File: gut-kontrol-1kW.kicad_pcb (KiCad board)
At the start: 2 copper layers, 119 x 85 mm, 49 parts, among them J1 PHASE_A, J2 PHASE_B, J3 PHASE_C, J4 VMOT, J5 GND, J7 Conn_01x12, Q1 IRFb4110N, Q2 IRFb4110N, Q3 IRFb4110N, Q4 IRFb4110N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

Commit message: Adding connector and CAD viz
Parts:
- added C11: 0.1 uF, Capacitor_SMD:C_0805_2012Metric_Pad1.18x1.45mm_HandSolder, F.Cu at (51.8, 59.1)
- added C12: 0.1 uF, Capacitor_SMD:C_0805_2012Metric_Pad1.18x1.45mm_HandSolder, F.Cu at (81.8, 59.1)
- added C13: 0.1 uF, Capacitor_SMD:C_0805_2012Metric_Pad1.18x1.45mm_HandSolder, F.Cu at (111.8, 59.1)
- added C14: 0.1 uF, Capacitor_SMD:C_0805_2012Metric_Pad1.18x1.45mm_HandSolder, F.Cu at (47.0, 59.7)
- added C15: 0.1 uF, Capacitor_SMD:C_0805_2012Metric_Pad1.18x1.45mm_HandSolder, F.Cu at (77.0, 59.7)
- added C16: 0.1 uF, Capacitor_SMD:C_0805_2012Metric_Pad1.18x1.45mm_HandSolder, F.Cu at (107.0, 59.7)
- added G***: LOGO, symbols:gut_25mm, F.Cu at (116.5, 119.2)
- added J10: PHASE_C_ISENSE, Connector_PinSocket_2.54mm:PinSocket_1x03_P2.54mm_Vertical, F.Cu at (108.3, 55.9)
- added J8: PHASE_A_ISENSE, Connector_PinSocket_2.54mm:PinSocket_1x03_P2.54mm_Vertical, F.Cu at (48.3, 55.9)
- added J9: PHASE_B_ISENSE, Connector_PinSocket_2.54mm:PinSocket_1x03_P2.54mm_Vertical, F.Cu at (78.3, 55.9)
- added R16: 100, Resistor_SMD:R_0805_2012Metric_Pad1.20x1.40mm_HandSolder, F.Cu at (49.5, 62.2)
- added R17: 100, Resistor_SMD:R_0805_2012Metric_Pad1.20x1.40mm_HandSolder, F.Cu at (79.5, 62.2)
- added R18: 100, Resistor_SMD:R_0805_2012Metric_Pad1.20x1.40mm_HandSolder, F.Cu at (109.5, 62.2)
- R15: renamed from R10; value 27 -> 10K
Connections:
- R15 pad 1: Net-(R10-Pad1) -> GND
- R15 pad 2: Net-(Q5-Pad1) -> Net-(Q6-Pad1)
- U2 pad 3: A_CURRENT_SENS -> Net-(R16-Pad1)
- U5 pad 3: B_CURRENT_SENS -> Net-(R17-Pad1)
- U6 pad 3: C_CURRENT_SENS -> Net-(R18-Pad1)
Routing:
- net Net-(R18-Pad1): track 0.00 -> 14.1 mm
- net Net-(R17-Pad1): track 0.00 -> 14.1 mm
- net Net-(R16-Pad1): track 0.00 -> 14.1 mm
- net GND: track 33.8 -> 43.6 mm, vias 13 -> 20
- net Net-(C13-Pad2): track 0.00 -> 6.43 mm
- net Net-(C11-Pad2): track 0.00 -> 6.43 mm
- net Net-(C12-Pad2): track 0.00 -> 6.43 mm
- net Net-(R11-Pad1): track 0.00 -> 4.54 mm
- net Net-(R10-Pad1): track 1.62 -> 4.79 mm, vias 1 -> 0
- net /PHASE_B: track 8.13 -> 7.33 mm
- net +48V: vias 0 -> 41
- added copper zone on B.Cu, net /PHASE_A_OUT
- added copper zone on B.Cu, net /PHASE_B_OUT
- added copper zone on B.Cu, net /PHASE_C_OUT
- added copper zone on F.Cu, net GND
- added copper zone on F.Cu, net HIN_A
- added copper zone on F.Cu, net HIN_B
- added copper zone on F.Cu, net HIN_C
- added copper zone on F.Cu, net LIN_A
- added copper zone on F.Cu, net LIN_B
- added copper zone on F.Cu, net LIN_C
- added copper zone on F.Cu, net Net-(C11-Pad2)
- added copper zone on F.Cu, net Net-(C12-Pad2)
- added copper zone on F.Cu, net Net-(C13-Pad2)
- added copper zone on F.Cu, net Net-(Q1-Pad1)
- added copper zone on F.Cu, net Net-(Q2-Pad1)
- added copper zone on F.Cu, net Net-(Q3-Pad1)
- added copper zone on F.Cu, net Net-(Q4-Pad1)
- added copper zone on F.Cu, net Net-(Q5-Pad1)
- added copper zone on F.Cu, net Net-(Q6-Pad1)
- added copper zone on F.Cu, net Net-(R16-Pad1)
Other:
- outline, holes or cut-outs redrawn
- board text added: "+ 3V3"
- board text added: "+12V"
- board text added: "A PWM"
- board text added: "B PWM"
- board text added: "C PWM"
- board text added: "GATE DRIVER"
- board text added: "GND"
- board text added: "GUT-KONTROL-1KW-v0.1 POWERSTAGE BOARD"

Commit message: some minor fix
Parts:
- C4: renamed from C6; value 2.2 uF -> 10 uF
- C5: renamed from C3; value 10 uF -> 2.2 uF
- R10: renamed from R12; value 10K -> 27
- R11: renamed from R13; value 10K -> 27
- renumbered C4 to C3, C5 to C6, R15 to R13, R8 to R9
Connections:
- C4 pad 1: /PHASE_C -> GND
- C4 pad 2: Net-(C6-Pad2) -> +3V3
- C5 pad 1: GND -> /PHASE_B
- C5 pad 2: +3V3 -> Net-(C5-Pad2)
- C6 pad 1: /PHASE_B -> /PHASE_C
- C6 pad 2: Net-(C5-Pad2) -> Net-(C6-Pad2)
- R10 pad 1: /PHASE_B -> Net-(R10-Pad1)
- R10 pad 2: Net-(Q3-Pad1) -> Net-(Q5-Pad1)
- R11 pad 1: GND -> Net-(R11-Pad1)
- R11 pad 2: Net-(Q4-Pad1) -> Net-(Q6-Pad1)
- R13 pad 2: Net-(Q6-Pad1) -> Net-(Q4-Pad1)
- R9 pad 1: Net-(R8-Pad1) -> Net-(R9-Pad1)
- R9 pad 2: Net-(Q3-Pad1) -> Net-(Q4-Pad1)
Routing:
- net +3V3: track 9.70 -> 23.9 mm, vias 0 -> 2
- net (no net): track 0.00 -> 8.50 mm, vias 0 -> 4
- net /PHASE_B: track 7.33 -> 9.55 mm
- net /PHASE_A: track 7.67 -> 9.89 mm
- net GND: track 43.6 -> 45.2 mm, vias 20 -> 21
- net /PHASE_C: track 8.94 -> 9.55 mm, vias 1 -> 0
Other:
- board text removed: "+ 3V3"
- board text removed: "+12V"
- board text removed: "A PWM"
- board text removed: "B PWM"
- board text removed: "C PWM"
- board text removed: "GND"

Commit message: major fix in conn footprint, bootsrap error, etc
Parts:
- removed the REF** at (105.0, 110.0)
- added U7: XT30PW-F, XT30PW-F:XT30PW-F, F.Cu at (156.6, 233.8)
- J7: footprint Connector_PinHeader_1.00mm:PinHeader_1x12_P1.00mm_Vertical -> Connector_PinHeader_2.54mm:PinHeader_1x12_P2.54mm_Vertical
- moved C1 165.1 mm to (173.8, 215.5)
- moved C10 165.0 mm to (257.1, 240.3)
- moved C11 165.0 mm to (165.9, 178.3)
- moved C12 165.0 mm to (195.9, 178.3)
- moved C13 165.0 mm to (225.9, 178.3)
- moved C2 165.0 mm to (173.1, 231.7)
- moved C3 165.0 mm to (203.1, 231.7)
- moved C5 165.0 mm to (203.8, 215.4)
- moved C6 165.0 mm to (233.8, 215.4)
- moved C7 165.0 mm to (257.1, 180.3)
- moved C8 165.0 mm to (257.1, 200.3)
- moved C9 165.0 mm to (257.1, 220.3)
- moved G*** 165.0 mm to (230.6, 238.5)
- moved J10 165.0 mm to (222.4, 175.2)
- moved J4 165.0 mm to (158.1, 205.3)
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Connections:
- J7 pad 1: +12V -> +3V3
- J7 pad 2: +12V -> +3V3
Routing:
- net +3V3: track 23.9 -> 11.9 mm, vias 2 -> 0
- net (no net): track 8.50 -> 0.00 mm, vias 4 -> 0
- net GND: track 45.2 -> 53.5 mm, vias 21 -> 24
- net HIN_A: track 37.3 -> 29.3 mm, vias 0 -> 2
- net LIN_A: track 36.2 -> 29.5 mm, vias 0 -> 2
- net +12V: track 56.5 -> 50.9 mm
- net HIN_C: track 38.2 -> 41.2 mm, vias 0 -> 2
- net HIN_B: track 16.6 -> 18.8 mm
- net Net-(D2-K): track 10.6 -> 12.7 mm
- net Net-(D3-K): track 10.6 -> 12.3 mm
- net LIN_B: track 17.2 -> 18.8 mm
- net Net-(D1-K): track 10.6 -> 11.8 mm
- net Net-(D2-A): track 3.44 -> 2.28 mm
- net Net-(D1-A): track 3.44 -> 2.28 mm
- net LIN_C: track 39.7 -> 40.5 mm, vias 0 -> 2
- removed copper zone on F.Cu, net HIN_A
- removed copper zone on F.Cu, net HIN_B
- removed copper zone on F.Cu, net HIN_C
- removed copper zone on F.Cu, net LIN_A
- removed copper zone on F.Cu, net LIN_B
- removed copper zone on F.Cu, net LIN_C
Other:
- board text added: "GUT-KONTROL-1KW-v0.2 POWERSTAGE BOARD"
- board text removed: "GUT-KONTROL-1KW-v0.1 POWERSTAGE BOARD"

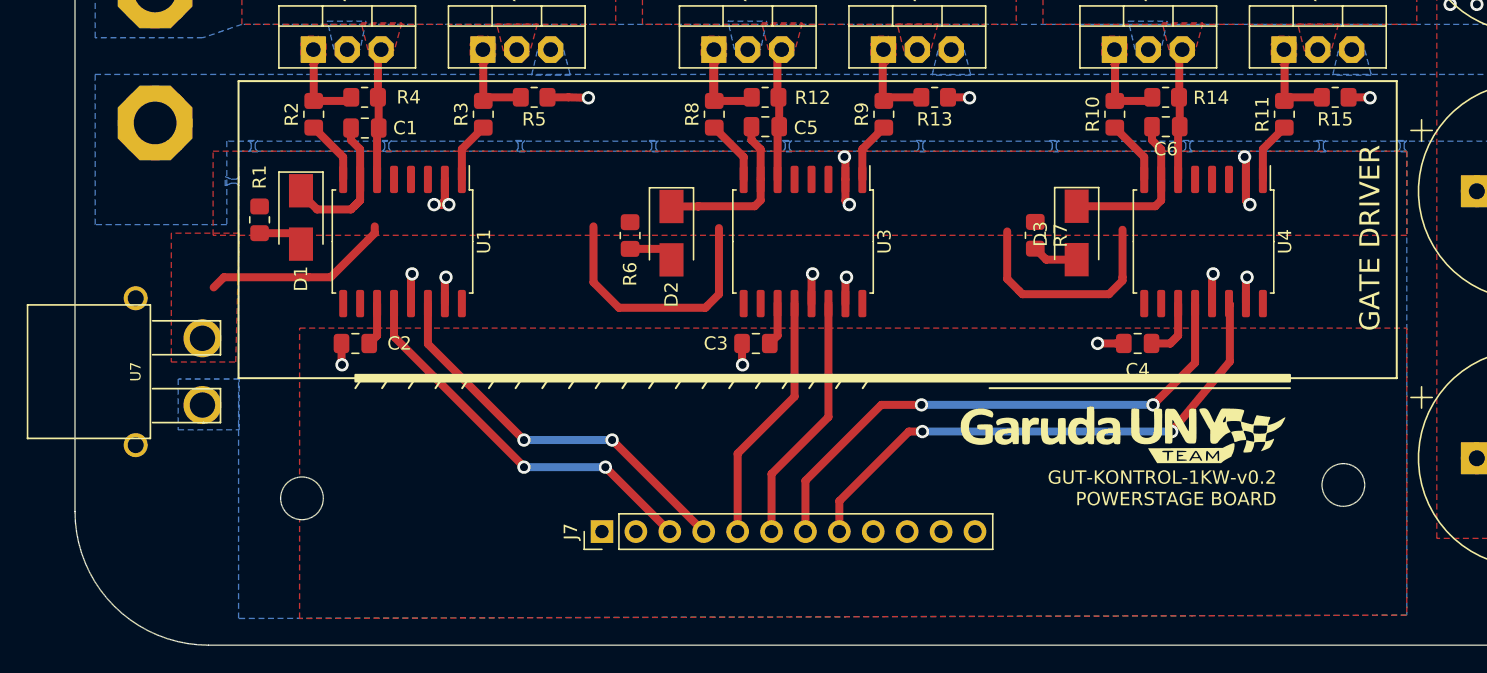
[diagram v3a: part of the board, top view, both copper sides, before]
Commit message: ganti heatsink
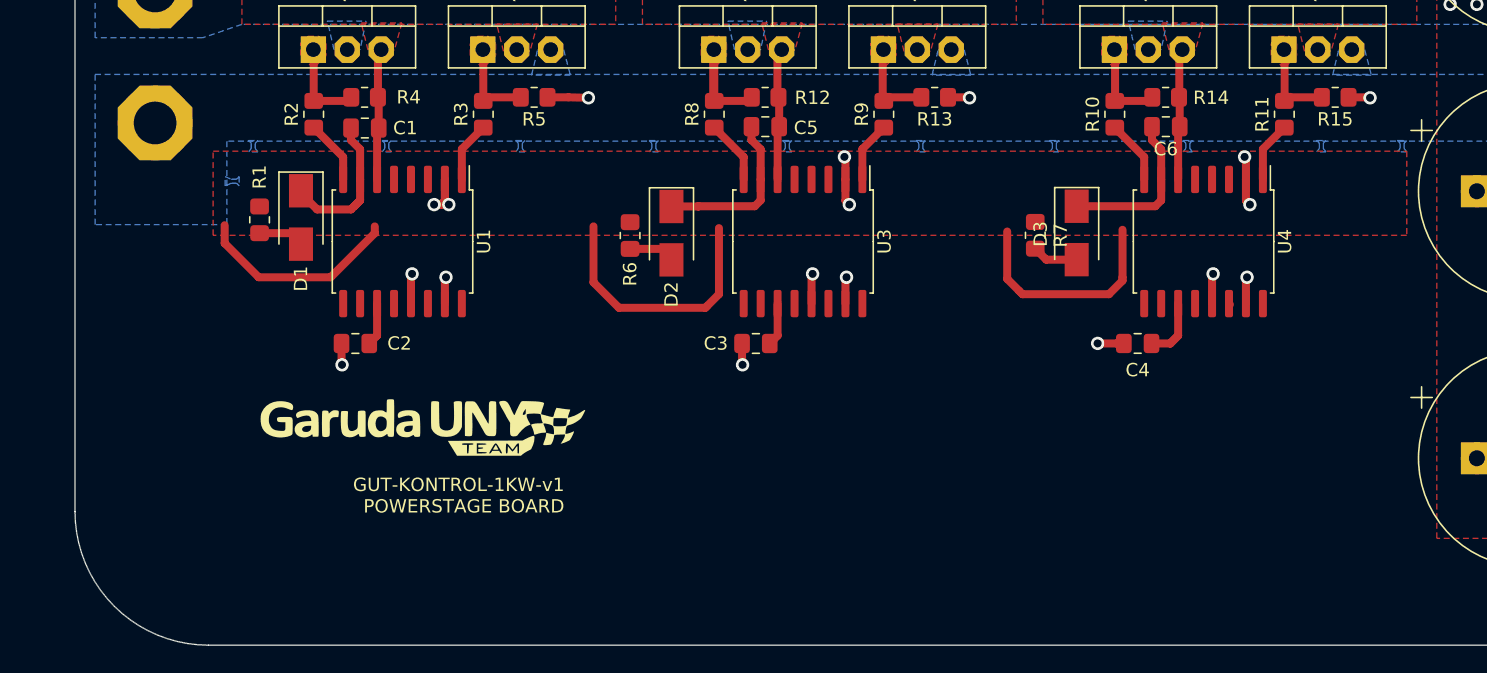
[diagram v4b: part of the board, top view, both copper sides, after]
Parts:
- removed J7: Conn_01x12, Connector_PinHeader_2.54mm:PinHeader_1x12_P2.54mm_Vertical
- removed REF** (x2): MountingHole_3.2mm_M3, MountingHole:MountingHole_3.2mm_M3
- removed U7: XT30PW-F, XT30PW-F:XT30PW-F
- moved G*** 52.4 mm to (178.2, 237.9)
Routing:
- net HIN_C: track 41.2 -> 0.00 mm, vias 2 -> 0
- net LIN_C: track 40.5 -> 0.09 mm, vias 2 -> 0
- net LIN_A: track 29.5 -> 0.00 mm, vias 2 -> 0
- net HIN_A: track 29.3 -> 0.00 mm, vias 2 -> 0
- net LIN_B: track 18.8 -> 0.00 mm
- net HIN_B: track 18.8 -> 0.00 mm
- net +12V: track 50.9 -> 52.2 mm
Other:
- board text added: "GUT-KONTROL-1KW-v1 POWERSTAGE BOARD"
- board text removed: "GATE DRIVER"
- board text removed: "GUT-KONTROL-1KW-v0.2 POWERSTAGE BOARD"

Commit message: Layout PCB
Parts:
- added ?: MountingHole_3.2mm_M3, MountingHole:MountingHole_3.2mm_M3, F.Cu at (248.3, 183.7)
- added ?: MountingHole_3.2mm_M3, MountingHole:MountingHole_3.2mm_M3, F.Cu at (156.3, 183.7)
- added ?: MountingHole_3.2mm_M3, MountingHole:MountingHole_3.2mm_M3, F.Cu at (248.3, 247.7)
- added ?: MountingHole_3.2mm_M3, MountingHole:MountingHole_3.2mm_M3, F.Cu at (160.8, 247.7)
- added CFF1: 33nF, Resistor_SMD:R_0805_2012Metric, F.Cu at (223.3, 249.0)
- added CIN1: 33uF/100W, Capacitor_THT:CP_Radial_D8.0mm_P3.50mm, F.Cu at (247.4, 240.9)
- added COUT1: 100uF/35V, Capacitor_THT:CP_Radial_D8.0mm_P3.50mm, F.Cu at (210.8, 241.0)
- added D4: S310, Diode_SMD:D_SMA, F.Cu at (236.7, 236.5)
- added J7: Conn_01x12, Connector_PinHeader_2.54mm:PinHeader_2x06_P2.54mm_Vertical, F.Cu at (157.9, 228.3)
- added L1: 100uH/1A, Inductor_SMD:L_10.4x10.4_H4.8, F.Cu at (223.7, 241.0)
- added R19: 26K, Resistor_SMD:R_0805_2012Metric, F.Cu at (227.8, 249.0)
- added R20: 3K, Resistor_SMD:R_0805_2012Metric, F.Cu at (219.1, 249.0)
- added U8: AMS1117-2.85, Package_TO_SOT_SMD:SOT-223-3_TabPin2, F.Cu at (211.0, 247.9)
- added XL1: ~, Package_TO_SOT_SMD:TO-252-5_TabPin3, F.Cu at (237.0, 246.0)
- moved G*** 4.46 mm to (179.1, 242.3)
- moved C10 0.69 mm to (257.1, 240.9)
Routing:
- net HIN_C: track 0.00 -> 101.8 mm, vias 0 -> 2
- net LIN_C: track 0.09 -> 85.9 mm
- net HIN_B: track 0.00 -> 76.9 mm, vias 0 -> 2
- net +12V: track 52.2 -> 110.1 mm, vias 0 -> 2
- net LIN_B: track 0.00 -> 55.0 mm
- net HIN_A: track 0.00 -> 36.6 mm, vias 0 -> 2
- net +3V3: track 11.9 -> 40.5 mm, vias 0 -> 2
- net LIN_A: track 0.00 -> 24.7 mm
- net Net-(XL1-FB): track 0.00 -> 24.6 mm
- net Net-(D4-K): track 0.00 -> 15.8 mm
- net GND: track 53.5 -> 65.5 mm, vias 24 -> 28

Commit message: revisi power plane + logo
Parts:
- removed the G*** at (179.1, 242.3)
- added G***: LOGO, symbols:modrive_16mm, F.Cu at (184.2, 243.5)
- moved ? 4.50 mm to (156.3, 247.7)
- moved U8 0.73 mm to (210.2, 248.0), turned to 180 degrees
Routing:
- net +12V: track 110.1 -> 66.6 mm, vias 2 -> 17
- net +3V3: track 40.5 -> 12.1 mm, vias 2 -> 16
- net GND: track 65.5 -> 65.2 mm, vias 28 -> 49
- added copper zone on B.Cu, net +12V
- added copper zone on B.Cu, net +3V3
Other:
- board size 119 x 85 mm -> 119.6 x 85 mm
- board text removed: "GUT-KONTROL-1KW-v1 POWERSTAGE BOARD"
